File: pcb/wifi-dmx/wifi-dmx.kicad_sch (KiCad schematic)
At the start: 5 parts, among them J1 Conn_01x16_Socket, J2 Conn_01x16_Socket, J3 USB4110GFA

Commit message: adding XLD connector
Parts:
- added J5: NC3FAH1, Connector_Audio:Jack_XLR_Neutrik_NC3FAH1_Horizontal, symbol Connector_Audio:NC3FAH1
- J3: footprint USB4110GFA:GCT_USB4110GFA -> footprints:GCT_USB4110GFA
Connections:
- net GND: now also J1.1 (Pin_1), J1.11 (Pin_11), J1.14 (Pin_14), J1.5 (Pin_5), J1.7 (Pin_7)
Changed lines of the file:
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@@
+	(wire
+		(pts
+			(xy 34.29 134.62) (xy 48.26 134.62)
+		)
+		(stroke
+			(width 0)
+			(type default)
+		)
+	)
+	(wire
+		(pts
+			(xy 34.29 149.86) (xy 48.26 149.86)
+		)
+		(stroke
+			(width 0)
+			(type default)
+		)
+	)
 	(wire
 		(pts
@@
 	(wire
 		(pts
+			(xy 34.29 139.7) (xy 48.26 139.7)
+		)
+		(stroke
+			(width 0)
+			(type default)
+		)
+	)
+	(wire
+		(pts
 			(xy 87.63 52.07) (xy 87.63 58.42)
 		)
@@
 	(wire
 		(pts
+			(xy 34.29 157.48) (xy 48.26 157.48)
+		)
+		(stroke
+			(width 0)
+			(type default)
+		)
+	)
+	(wire
+		(pts
 			(xy 86.36 124.46) (xy 102.87 124.46)
 		)
@@
 		(pts
 			(xy 77.47 52.07) (xy 87.63 52.07)
+		)
+		(stroke
+			(width 0)
+			(type default)
+		)
+	)
+	(wire
+		(pts
+			(xy 34.29 124.46) (xy 48.26 124.46)
 		)
 		(stroke
@@
 		)
 	)
+	(global_label "GND"
+		(shape input)
+		(at 34.29 149.86 180)
+		(fields_autoplaced yes)
+		(effects
+			(font
+				(size 1.27 1.27)
+			)
+			(justify right)
+		)
+		(property "Intersheetrefs" "${INTERSHEET_REFS}"
+			(at 27.4343 149.86 0)
+			(effects
+				(font
+					(size 1.27 1.27)
+				)
+				(justify right)
+				(hide yes)
+			)
+		)
+	)
 	(global_label "VCC_5V"
 		(shape output)
@@
 		)
 	)
+	(global_label "GND"
+		(shape input)
+		(at 34.29 124.46 180)
+		(fields_autoplaced yes)
+		(effects
+			(font
+				(size 1.27 1.27)
+			)
+			(justify right)
+		)
+		(property "Intersheetrefs" "${INTERSHEET_REFS}"
+			(at 27.4343 124.46 0)
+			(effects
+				(font
+					(size 1.27 1.27)
+				)
+				(justify right)
+				(hide yes)
+			)
+		)
+	)
+	(global_label "GND"
+		(shape input)
+		(at 34.29 134.62 180)
+		(fields_autoplaced yes)
+		(effects
+			(font
+				(size 1.27 1.27)
+			)
+			(justify right)
+		)
+		(property "Intersheetrefs" "${INTERSHEET_REFS}"
+			(at 27.4343 134.62 0)
+			(effects
+				(font
+					(size 1.27 1.27)
+				)
+				(justify right)
+				(hide yes)
+			)
+		)
+	)
 	(global_label "D+"
 		(shape input)
@@
 		)
 	)
+	(global_label "GND"
+		(shape input)
+		(at 34.29 157.48 180)
+		(fields_autoplaced yes)
+		(effects
+			(font
+				(size 1.27 1.27)
+			)
+			(justify right)
+		)
+		(property "Intersheetrefs" "${INTERSHEET_REFS}"
+			(at 27.4343 157.48 0)
+			(effects
+				(font
+					(size 1.27 1.27)
+				)
+				(justify right)
+				(hide yes)
+			)
+		)
+	)
 	(global_label "VCC_5V"
 		(shape input)
@@
 				)
 				(justify left)
+				(hide yes)
+			)
+		)
+	)
+	(global_label "GND"
+		(shape input)
+		(at 34.29 139.7 180)
+		(fields_autoplaced yes)
+		(effects
+			(font
+				(size 1.27 1.27)
+			)
+			(justify right)
+		)
+		(property "Intersheetrefs" "${INTERSHEET_REFS}"
+			(at 27.4343 139.7 0)
+			(effects
+				(font
+					(size 1.27 1.27)
+				)
+				(justify right)
 				(hide yes)
 			)
@@
 	)
 	(symbol
+		(lib_id "Connector_Audio:NC3FAH1")
+		(at 200.66 50.8 0)
+		(unit 1)
+		(exclude_from_sim no)
+		(in_bom yes)
+		(on_board yes)
+		(dnp no)
+		(fields_autoplaced yes)
+		(property "Reference" "J5"
+			(at 200.66 40.64 0)
+			(effects
+				(font
+					(size 1.27 1.27)
+				)
+			)
+		)
+		(property "Value" "NC3FAH1"
+			(at 200.66 43.18 0)
+			(effects
+				(font
+					(size 1.27 1.27)
+				)
+			)
+		)
+		(property "Footprint" "Connector_Audio:Jack_XLR_Neutrik_NC3FAH1_Horizontal"
+			(at 200.66 50.8 0)
+			(effects
+				(font
+					(size 1.27 1.27)
+				)
+				(hide yes)
+			)
+		)
+		(property "Datasheet" "https://www.neutrik.com/en/product/nc3fah1"
+			(at 200.66 50.8 0)
+			(effects
+				(font
+					(size 1.27 1.27)
+				)
+				(hide yes)
+			)
+		)
+		(property "Description" "A Series, 3 pole female XLR receptacle, grounding: mating connector shell to pin1 and front panel, horizontal PCB mount"
+			(at 200.66 50.8 0)
+			(effects
+				(font
+					(size 1.27 1.27)
+				)
+				(hide yes)
+			)
+		)
+		(pin "3"
+		)
+		(pin "2"
+		)
+		(pin "1"
+		)
+		(instances
+			(project ""
+				(path "/71c79178-6928-40ce-8b54-dc66c35d9959"
+					(reference "J5")
+					(unit 1)
+				)
+			)
+		)
+	)
+	(symbol
 		(lib_id "USB:USB4110GFA")
 		(at 59.69 54.61 0)
@@
 			)
 		)
-		(property "Footprint" "USB4110GFA:GCT_USB4110GFA"
+		(property "Footprint" "footprints:GCT_USB4110GFA"
 			(at 59.69 54.61 0)
 			(effects

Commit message: finishing schematic and organizing pcb
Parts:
- added C1: 0u1F, Capacitor_SMD:C_0402_1005Metric, symbol Device:C
- added U1: MAX485E, Package_SO:SOIC-8_3.9x4.9mm_P1.27mm, symbol Interface_UART:MAX485E
- J1, J2: footprint (none) -> Connector_PinHeader_2.54mm:PinHeader_1x16_P2.54mm_Vertical
- J3: MOUSER_PART_NUMBER (none) -> 640-USB4110-GF-A
- R1, R2: footprint (none) -> Resistor_SMD:R_0402_1005Metric; MOUSER_PART_NUMBER (none) -> 71-CRCW0402-5.1K-E3
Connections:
- net GND: now also J5.1, C1.2, U1.5 (GND)
- net VCC_5V: now also C1.1, U1.2 (~{RE}), U1.3 (DE), U1.8 (VCC)
- net at J5.2: now also U1.7 (B)
- net at J5.3: now also U1.6 (A)
- net TXD1: now reaches J1.12 (Pin_12)
- net TXD1: now also U1.4 (DI)
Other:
- moved on the sheet: J3, J5, R1, R2

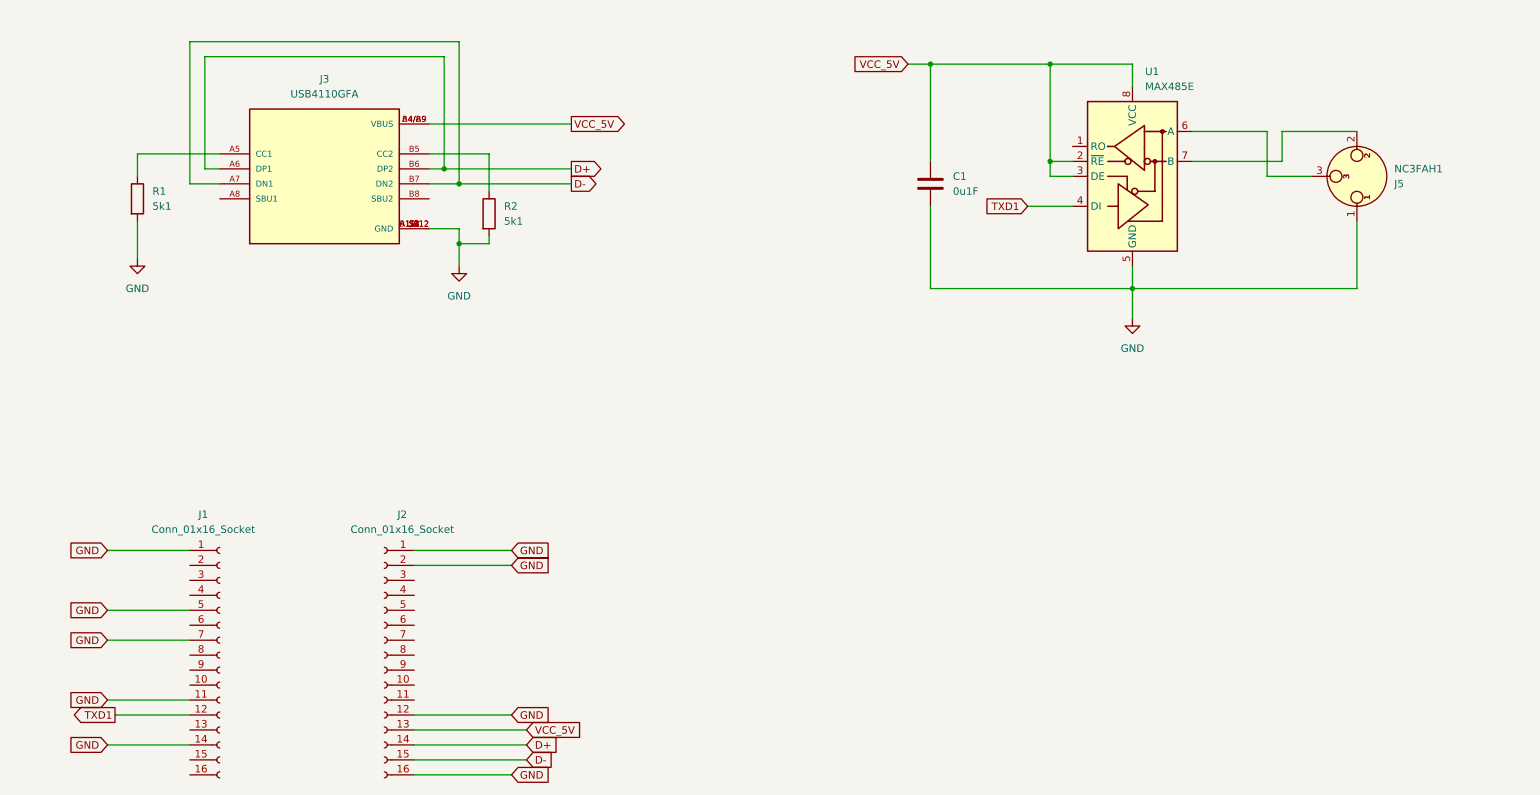
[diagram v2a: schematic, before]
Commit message: adding button and led to pcb
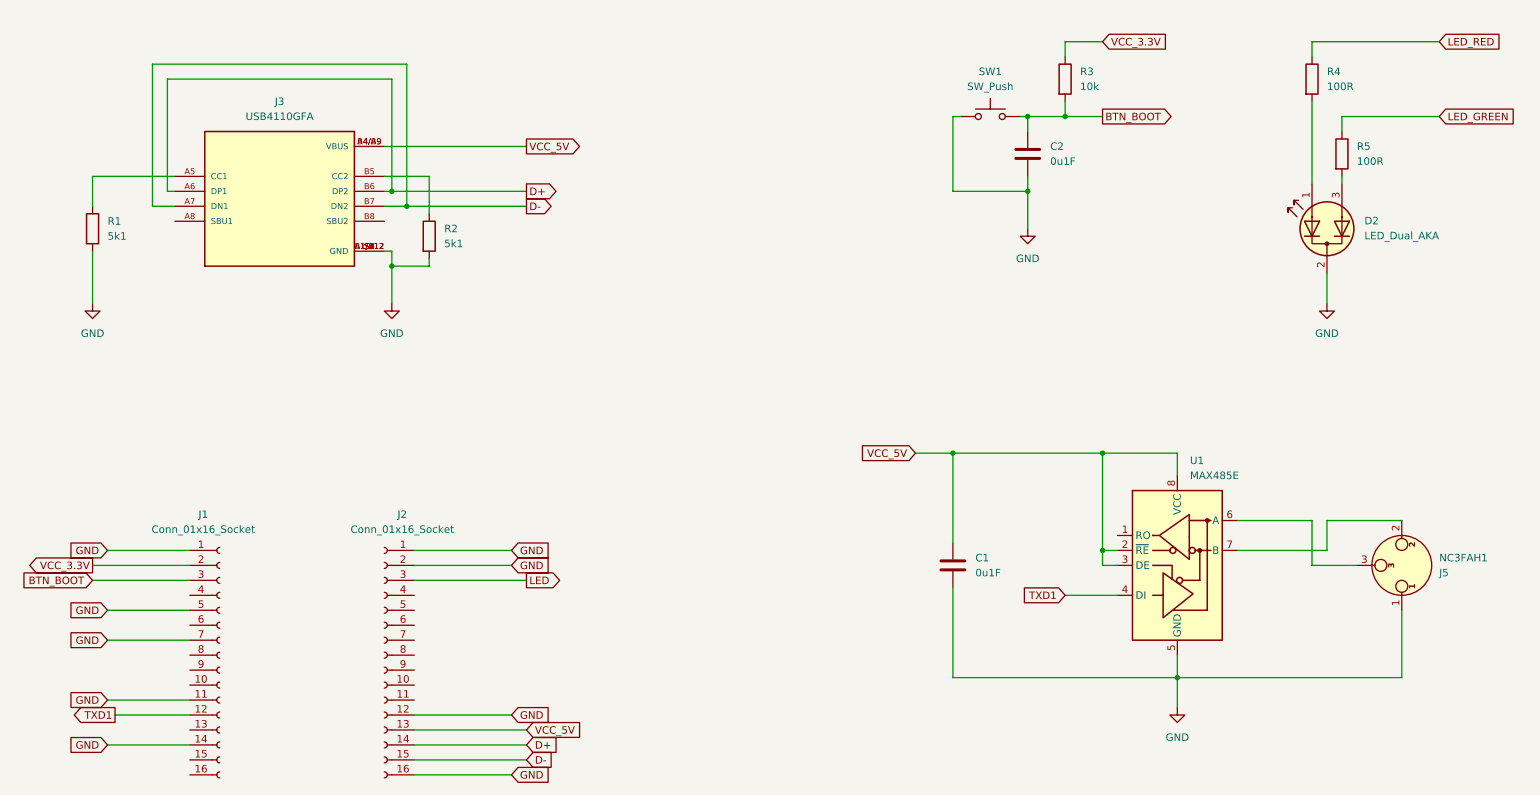
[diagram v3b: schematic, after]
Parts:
- added C2: 0u1F, Capacitor_SMD:C_0402_1005Metric, symbol Device:C
- added D2: LED_Dual_AKA, LED_THT:LED_D5.0mm-3_Horizontal_O3.81mm_Z3.0mm, symbol Device:LED_Dual_AKA
- added R3: 10k, Resistor_SMD:R_0402_1005Metric, symbol Device:R
- added R4, R5: 100R, symbol Device:R
- added SW1: SW_Push, Button_Switch_THT:SW_Tactile_SPST_Angled_PTS645Vx58-2LFS, symbol Switch:SW_Push
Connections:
- net GND: now also C2.2, D2.2 (K), SW1.1
- net LED: now reaches J2.3 (Pin_3)
- net VCC_3.3V: now reaches J1.2 (Pin_2)
- net VCC_3.3V: now also R3.1
- net BTN_BOOT: now reaches J1.3 (Pin_3)
- net BTN_BOOT: now also C2.1, R3.2, SW1.2
- new net: D2.3 (A2), R5.2
- new net: D2.1 (A1), R4.2
- new net LED_GREEN: R5.1
- new net LED_RED: R4.1
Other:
- moved on the sheet: C1, J3, J5, R1, R2, U1

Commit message: finishing schematic, finishing pcb, integrating pcb-stl with enclosure
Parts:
- C1, C2: footprint Capacitor_SMD:C_0402_1005Metric -> Capacitor_SMD:C_0402_1005Metric_Pad0.74x0.62mm_HandSolder
- J1, J2: MOUSER_PART_NUMBER (none) -> 200-SSW11601TS
- R1, R2, R3: footprint Resistor_SMD:R_0402_1005Metric -> Resistor_SMD:R_0402_1005Metric_Pad0.72x0.64mm_HandSolder
- R4, R5: value 100R -> 75R; footprint (none) -> Resistor_SMD:R_0402_1005Metric_Pad0.72x0.64mm_HandSolder; MOUSER_PART_NUMBER (none) -> 71-CRCW040275R0JNEDC
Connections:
- net LED is gone; now on net LED_RED: J2.3 (Pin_3)
- net LED_GREEN: now also J2.4 (Pin_4)
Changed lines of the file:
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@@
+	(wire
+		(pts
+			(xy 86.36 132.08) (xy 105.41 132.08)
+		)
+		(stroke
+			(width 0)
+			(type default)
+		)
+	)
 	(wire
 		(pts
@@
 		)
 	)
-	(global_label "LED"
+	(global_label "LED_RED"
 		(shape output)
 		(at 105.41 129.54 0)
@@
 		)
 		(property "Intersheetrefs" "${INTERSHEET_REFS}"
-			(at 111.8423 129.54 0)
+			(at 116.4989 129.54 0)
 			(effects
 				(font
@@
 		(property "Intersheetrefs" "${INTERSHEET_REFS}"
 			(at 115.2895 154.94 0)
+			(effects
+				(font
+					(size 1.27 1.27)
+				)
+				(justify left)
+				(hide yes)
+			)
+		)
+	)
+	(global_label "LED_GREEN"
+		(shape output)
+		(at 105.41 132.08 0)
+		(fields_autoplaced yes)
+		(effects
+			(font
+				(size 1.27 1.27)
+			)
+			(justify left)
+		)
+		(property "Intersheetrefs" "${INTERSHEET_REFS}"
+			(at 118.9784 132.08 0)
 			(effects
 				(font
@@
 			)
 		)
-		(property "MOUSER_PART_NUMBER" ""
+		(property "MOUSER_PART_NUMBER" "200-SSW11601TS"
 			(at 81.28 142.24 0)
 			(effects
@@
 			)
 		)
-		(property "Value" "100R"
+		(property "Value" "75R"
 			(at 246.38 58.4199 0)
 			(effects
@@
 			)
 		)
-		(property "Footprint" ""
+		(property "Footprint" "Resistor_SMD:R_0402_1005Metric_Pad0.72x0.64mm_HandSolder"
 			(at 242.062 57.15 90)
 			(effects
@@
 		)
 		(property "Description" "Resistor"
+			(at 243.84 57.15 0)
+			(effects
+				(font
+					(size 1.27 1.27)
+				)
+				(hide yes)
+			)
+		)
+		(property "MOUSER_PART_NUMBER" "71-CRCW040275R0JNEDC "
 			(at 243.84 57.15 0)
 			(effects
@@
 			)
 		)
-		(property "Value" "100R"
+		(property "Value" "75R"
 			(at 241.3 45.7199 0)
 			(effects
@@
 			)
 		)
-		(property "Footprint" ""
+		(property "Footprint" "Resistor_SMD:R_0402_1005Metric_Pad0.72x0.64mm_HandSolder"
 			(at 236.982 44.45 90)
 			(effects
@@
 		)
 		(property "Description" "Resistor"
+			(at 238.76 44.45 0)
+			(effects
+				(font
+					(size 1.27 1.27)
+				)
+				(hide yes)
+			)
+		)
+		(property "MOUSER_PART_NUMBER" "71-CRCW040275R0JNEDC "
 			(at 238.76 44.45 0)
 			(effects
@@
 			)
 		)
-		(property "Footprint" "Capacitor_SMD:C_0402_1005Metric"
+		(property "Footprint" "Capacitor_SMD:C_0402_1005Metric_Pad0.74x0.62mm_HandSolder"
 			(at 178.7652 130.81 0)
 			(effects
@@
 			)
 		)
-		(property "Footprint" "Capacitor_SMD:C_0402_1005Metric"
+		(property "Footprint" "Capacitor_SMD:C_0402_1005Metric_Pad0.74x0.62mm_HandSolder"
 			(at 191.4652 60.96 0)
 			(effects
@@
 			)
 		)
-		(property "Footprint" "Resistor_SMD:R_0402_1005Metric"
+		(property "Footprint" "Resistor_SMD:R_0402_1005Metric_Pad0.72x0.64mm_HandSolder"
 			(at 195.072 44.45 90)
 			(effects
@@
 			)
 		)
-		(property "Footprint" "Resistor_SMD:R_0402_1005Metric"
+		(property "Footprint" "Resistor_SMD:R_0402_1005Metric_Pad0.72x0.64mm_HandSolder"
 			(at 87.122 71.12 90)
 			(effects
@@
 			)
 		)
-		(property "Footprint" "Resistor_SMD:R_0402_1005Metric"
+		(property "Footprint" "Resistor_SMD:R_0402_1005Metric_Pad0.72x0.64mm_HandSolder"
 			(at 29.972 69.85 90)
 			(effects
@@
 			)
 		)
-		(property "MOUSER_PART_NUMBER" ""
+		(property "MOUSER_PART_NUMBER" "200-SSW11601TS"
 			(at 53.34 142.24 0)
 			(effects

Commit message: hiding mouser part numbers in schematic
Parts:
- D2: MOUSER_PART_NUMBER (none) -> 442-BLBUBGE204
- J5: MOUSER_PART_NUMBER (none) -> 568-NC3FAH1
- SW1: MOUSER_PART_NUMBER (none) -> 611-PTS645VL582
- U1: MOUSER_PART_NUMBER (none) -> 700-MAX485CUA
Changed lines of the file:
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@@
+			)
+		)
+		(property "MOUSER_PART_NUMBER" "568-NC3FAH1"
+			(at 254 127 0)
+			(effects
+				(font
+					(size 1.27 1.27)
+				)
+				(hide yes)
 			)
 		)
@@
 			)
 		)
+		(property "MOUSER_PART_NUMBER" "700-MAX485CUA"
+			(at 215.9 127 0)
+			(effects
+				(font
+					(size 1.27 1.27)
+				)
+				(hide yes)
+			)
+		)
 		(pin "1"
 		)
@@
 			)
 		)
+		(property "MOUSER_PART_NUMBER" "611-PTS645VL582"
+			(at 184.15 50.8 0)
+			(effects
+				(font
+					(size 1.27 1.27)
+				)
+				(hide yes)
+			)
+		)
 		(pin "1"
 		)
@@
 			(at 241.3 69.85 0)
 			(effects
+				(font
+					(size 1.27 1.27)
+				)
+				(hide yes)
+			)
+		)
+		(property "MOUSER_PART_NUMBER" "442-BLBUBGE204"
+			(at 241.3 69.85 0)
+			(effects
